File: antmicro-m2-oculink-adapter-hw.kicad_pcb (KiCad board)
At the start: 4 copper layers, 22 x 80 mm, 15 parts, among them J1 PCB-Edge_M.2_Key-M, J2 OCuLink_x4_Amphenol_G14A42121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

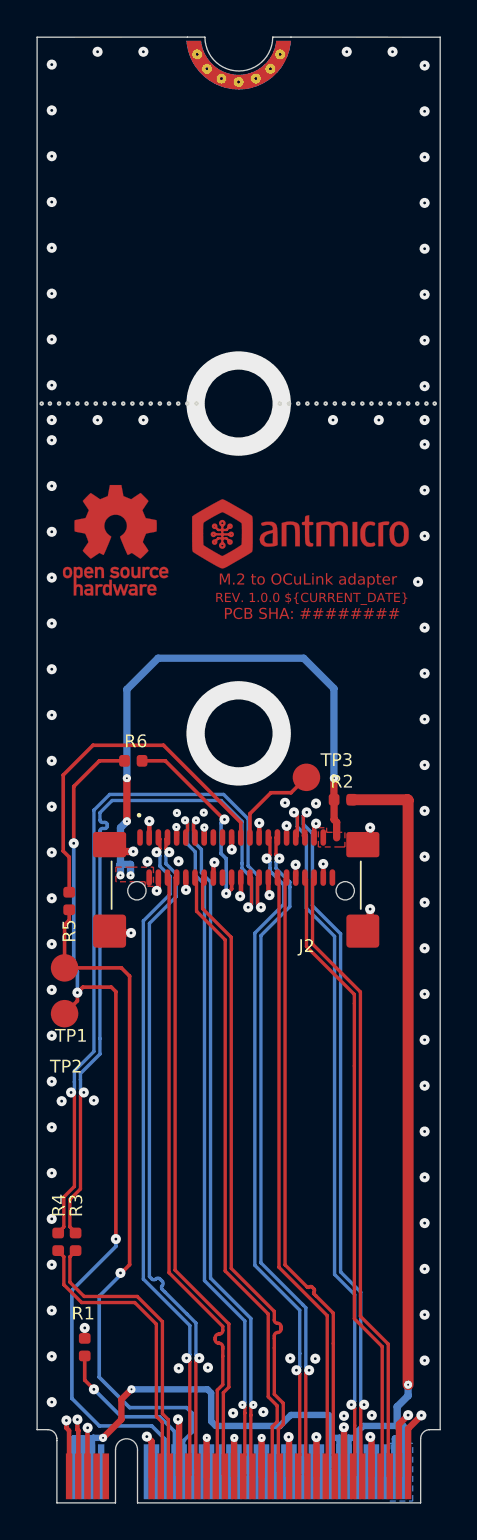
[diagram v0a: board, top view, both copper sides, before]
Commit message: [#80280] Clean up tracks, change gnd cutout size, fix drc errors, add more vias, move antmicro logo, change text size
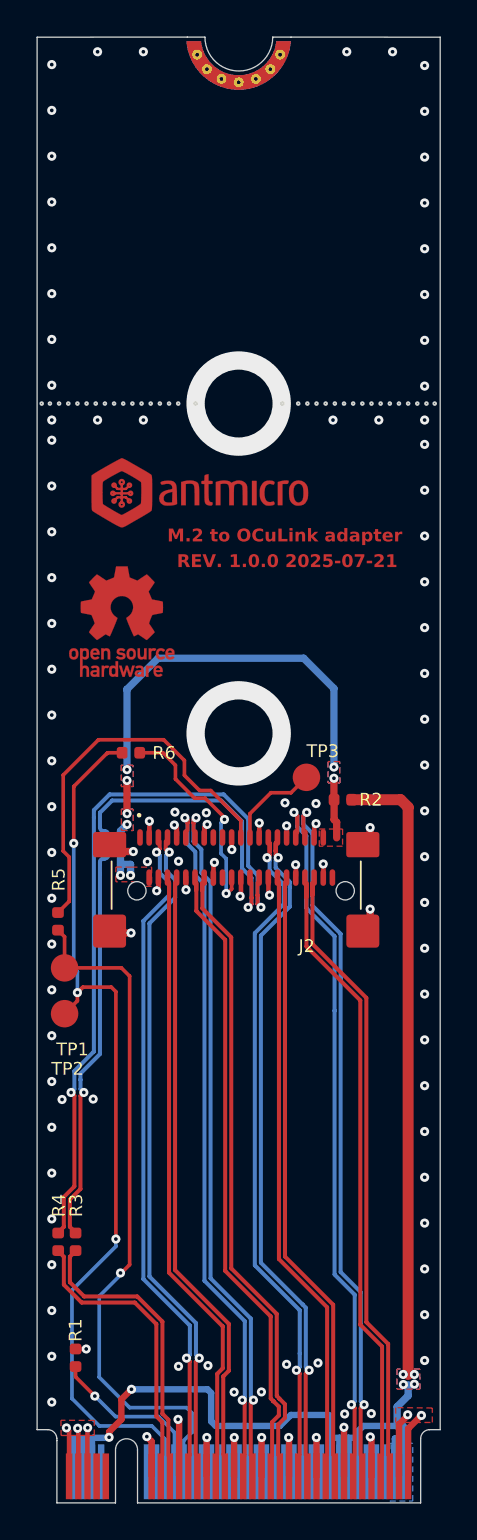
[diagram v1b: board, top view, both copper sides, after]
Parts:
- moved REF** 5.93 mm to (144.0, 75.5)
- moved REF** 4.45 mm to (139.8, 82.5) (x2)
- moved R5 1.27 mm to (136.3, 98.9)
- moved R1 0.77 mm to (137.2, 122.7)
- moved R6 0.46 mm to (140.3, 89.7)
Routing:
- net /~{PERSTC}: track 19.5 -> 21.6 mm
- net +3V3: track 32.5 -> 30.6 mm, vias 5 -> 8
- net /PCIe_{x4}.TX3+: track 39.3 -> 37.7 mm
- net /PCIe_{x4}.TX0+: track 37.1 -> 35.6 mm
- net /PCIe_{x4}.TX3-: track 39.2 -> 37.8 mm
- net /PCIe_{x4}.TX0-: track 37.1 -> 35.7 mm
- net /PCIe_{x4}.RX0-: track 34.1 -> 33.0 mm
- net /PCIe_{x4}.RX0+: track 34.1 -> 33.0 mm
- net /PCIe_{x4}.RX1+: track 34.8 -> 33.7 mm
- net /~{PERST}: track 38.9 -> 37.8 mm
- net /PCIe_{x4}.RX1-: track 34.7 -> 33.7 mm
- net /PCIe_{x4}.RX3-: track 34.6 -> 33.6 mm
- net /PCIe_{x4}.RX3+: track 34.6 -> 33.8 mm
- net /~{WAKEC}: track 11.2 -> 11.9 mm
- net Net-(J1-3.3V-Pad12): track 78.6 -> 78.0 mm, vias 3 -> 6
- added copper zone on B.Cu, net +3V3
- added copper zone on F.Cu, net GND
- added copper zone on F.Cu, net Net-(J1-3.3V-Pad12)
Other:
- outline, holes or cut-outs redrawn
- board text added: "REV. 1.0.0 2025-07-21"
- board text removed: "REV. ${REVISION} ${CURRENT_DATE}"

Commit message: [#80747] Clean up tracks
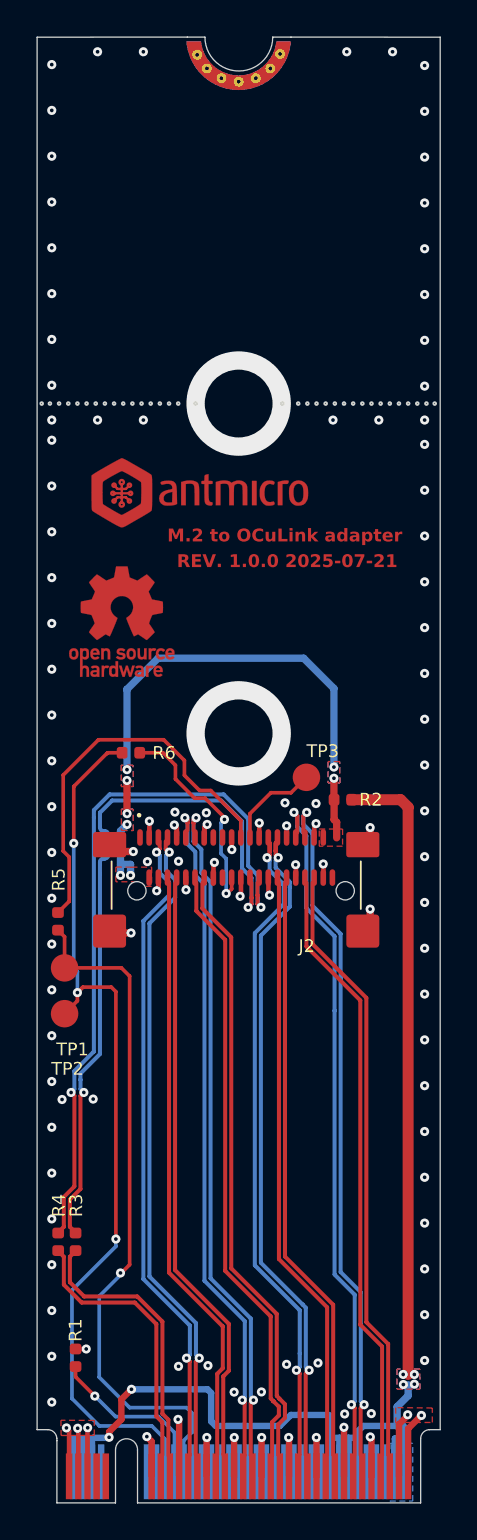
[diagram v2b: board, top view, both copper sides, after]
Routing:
- net /PCIe_{x4}.RX3+: track 33.8 -> 32.9 mm
- net /PCIe_{x4}.RX2+: track 33.1 -> 32.3 mm
- net /PCIe_{x4}.RX3-: track 33.6 -> 32.9 mm
- net /PCIe_{x4}.RX2-: track 33.0 -> 32.3 mm
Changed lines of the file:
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@@
 		)
 		(pad "1" thru_hole circle
-			(at -2.263505 0.937574)
+			(at -2.263505 0.947574)
 			(size 0.55 0.55)
 			(drill 0.2)
@@
 		)
 		(pad "1" thru_hole circle
-			(at -1.732412 1.732412)
+			(at -1.732412 1.692412)
 			(size 0.55 0.55)
 			(drill 0.2)
@@
 		)
 		(pad "1" thru_hole circle
-			(at -0.937574 2.263505)
+			(at -0.937574 2.223505)
 			(size 0.55 0.55)
 			(drill 0.2)
@@
 		)
 		(pad "1" thru_hole circle
-			(at 0 2.45)
+			(at 0 2.41)
 			(size 0.55 0.55)
 			(drill 0.2)
@@
 		)
 		(pad "1" smd custom
-			(at 0 2.45)
+			(at 0 2.46)
 			(size 0.55 0.55)
 			(layers "F.Cu" "F.Mask")
@@
 		)
 		(pad "1" smd custom
-			(at 0 2.45)
+			(at 0 2.46)
 			(size 0.55 0.55)
 			(layers "B.Cu" "B.Mask")
@@
 		)
 		(pad "1" thru_hole circle
-			(at 0.937574 2.263505)
+			(at 0.937574 2.223505)
 			(size 0.55 0.55)
 			(drill 0.2)
@@
 		)
 		(pad "1" thru_hole circle
-			(at 1.732412 1.732412)
+			(at 1.732412 1.692412)
 			(size 0.55 0.55)
 			(drill 0.2)
@@
 		)
 		(pad "1" thru_hole circle
-			(at 2.263505 0.937574)
+			(at 2.263505 0.897574)
 			(size 0.55 0.55)
 			(drill 0.2)
@@
 			(type default)
 		)
+		(locked yes)
 		(layer "Edge.Cuts")
 	)
@@
 			(type default)
 		)
+		(locked yes)
 		(layer "Edge.Cuts")
 	)
@@
 			(type default)
 		)
+		(locked yes)
 		(layer "Edge.Cuts")
 	)
@@
 			(type default)
 		)
+		(locked yes)
 		(layer "Edge.Cuts")
 	)
@@
 			(type default)
 		)
+		(locked yes)
 		(layer "Edge.Cuts")
 	)
@@
 	)
 	(segment
-		(start 148.35 96.75553)
-		(end 148.35 97.564469)
-		(width 0.22)
-		(layer "F.Cu")
-		(net 4)
-	)
-	(segment
 		(start 148.35 117.293346)
 		(end 150.98 119.923346)
@@
 	)
 	(segment
-		(start 150.18 97.438185)
-		(end 150.18 96.75553)
-		(width 0.22)
-		(layer "F.Cu")
-		(net 6)
-	)
-	(segment
 		(start 153.12 103.036654)
 		(end 153.12 120.736654)
@@
 	)
 	(segment
-		(start 142.68 97.180012)
-		(end 142.68 96.76)
-		(width 0.22)
-		(layer "F.Cu")
-		(net 7)
-	)
-	(segment
 		(start 142.68 117.896654)
 		(end 145.615 120.831654)
@@
 	)
 	(segment
-		(start 149.85 97.564469)
-		(end 149.85 96.75553)
-		(width 0.22)
-		(layer "F.Cu")
-		(net 9)
-	)
-	(segment
 		(start 153.979 122.062346)
 		(end 153.979 127.989345)
@@
 	(segment
 		(start 148.68 96.75553)
-		(end 148.68 97.438185)
-		(width 0.22)
-		(layer "F.Cu")
-		(net 14)
-	)
-	(segment
-		(start 148.68 96.75553)
 		(end 148.68 117.156654)
 		(width 0.22)
@@
 	)
 	(segment
-		(start 143.84 97.16475)
-		(end 143.84 96.759988)
-		(width 0.22)
-		(layer "F.Cu")
-		(net 16)
-	)
-	(segment
 		(start 147.899 124.897105)
 		(end 148.0445 125.042604)
@@
 	)
 	(segment
-		(start 142.35 97.164762)
-		(end 142.35 96.76)
-		(width 0.22)
-		(layer "F.Cu")
-		(net 27)
-	)
-	(segment
 		(start 148.3755 124.911448)
 		(end 148.6755 125.211448)
@@
 		(width 0.22)
 		(layer "F.Cu")
-		(net 28)
-	)
-	(segment
-		(start 144.17 97.18)
-		(end 144.17 96.759988)
-		(width 0.22)
-		(layer "F.Cu")

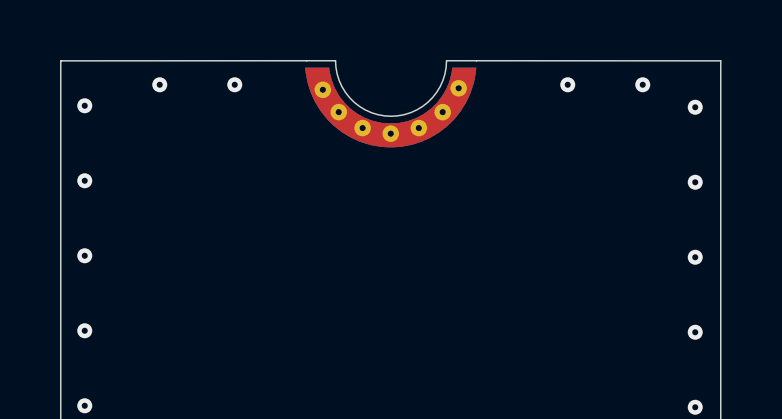
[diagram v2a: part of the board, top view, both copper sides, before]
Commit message: [#80747] Replace edge drill footprint
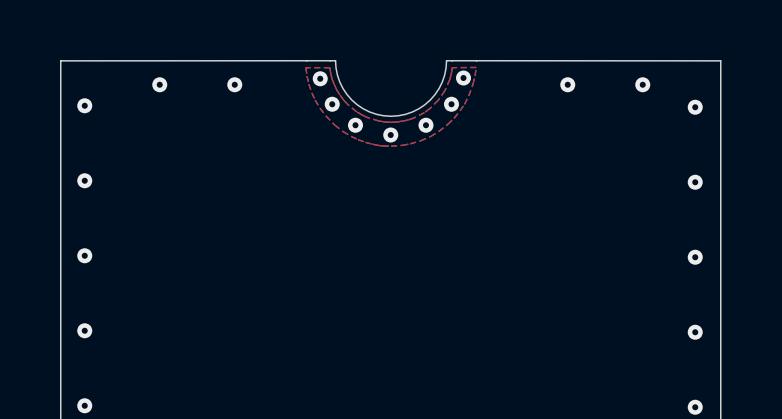
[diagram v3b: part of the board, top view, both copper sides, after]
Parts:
- removed the REF** at (146.2, 50.6)
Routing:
- net GND: vias 120 -> 127
- added copper zone on B.Cu, net GND
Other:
- outline, holes or cut-outs redrawn

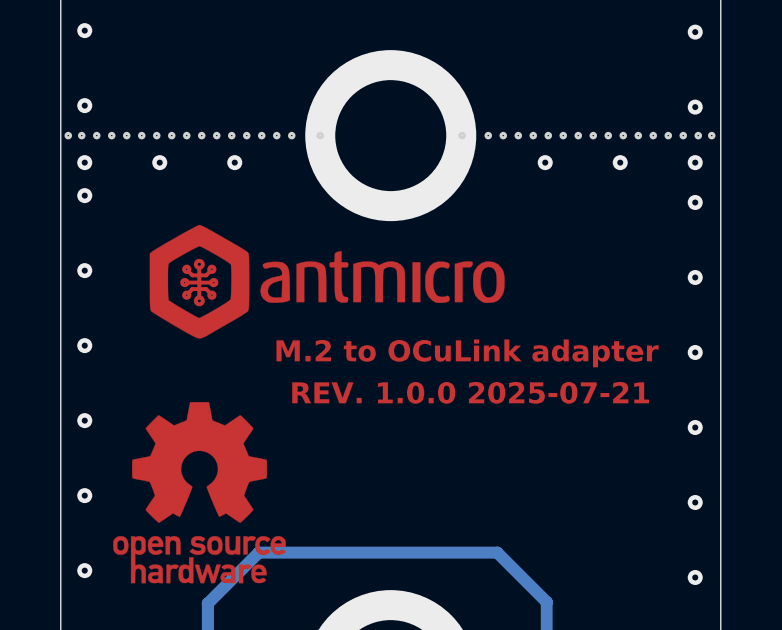
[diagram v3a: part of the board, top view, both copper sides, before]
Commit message: [#80747] change antmicro logo and correct date format
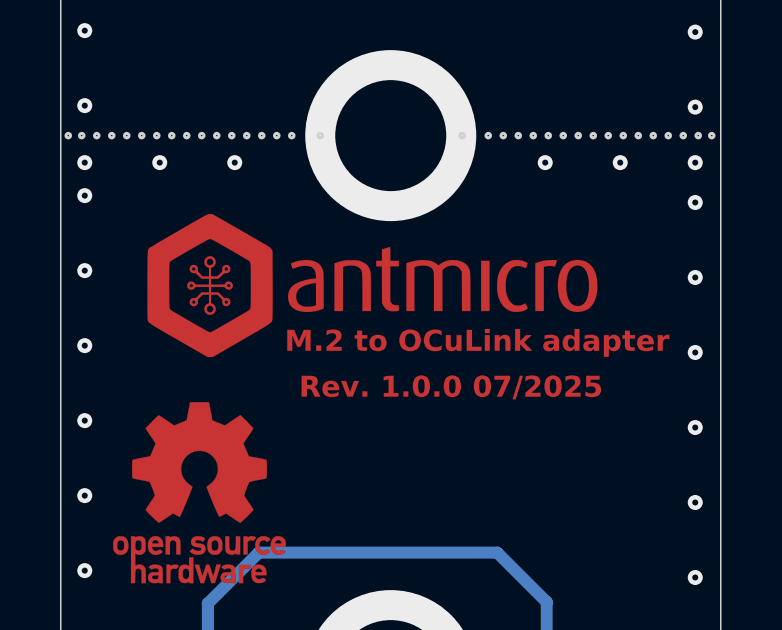
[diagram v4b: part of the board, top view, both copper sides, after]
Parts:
- removed the REF** at (144.0, 75.5)
- added REF**: antmicro-logo_scaled_15mm, antmicro-footprints:antmicro-logo_scaled_15mm, F.Cu at (146.0, 75.7)
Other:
- board text added: "Rev. 1.0.0 07/2025"
- board text removed: "REV. 1.0.0 2025-07-21"

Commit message: [#80747] Fix DRC
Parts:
- moved REF** 1.06 mm to (140.2, 83.5) (x2)
- moved REF** 0.28 mm to (146.0, 75.4)
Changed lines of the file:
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@@
 	(footprint "antmicro-footprints:antmicro-logo_scaled_15mm"
 		(layer "F.Cu")
-		(at 145.99 75.67)
+		(at 146.005 75.395)
 		(property "Reference" "REF**"
 			(at 0.1 -3 0)
@@
 	(footprint "antmicro-footprints:OSHW-Logo_5.7x6mm_Mask"
 		(layer "F.Cu")
-		(at 139.77 82.5)
+		(at 140.175 83.475)
 		(descr "Open Source Hardware Logo")
 		(tags "Logo OSHW")
@@
 	(footprint "antmicro-footprints:OSHW-Logo_5.7x6mm_Copper"
 		(layer "F.Cu")
-		(at 139.77 82.5)
+		(at 140.175 83.475)
 		(descr "Open Source Hardware Logo")
 		(tags "Logo OSHW")
@@
 	)
 	(gr_text "${TITLE}"
-		(at 148.86 77.45 0)
+		(at 148.65 77.25 0)
 		(layer "F.Cu")
 		(effects
@@
 	)
 	(gr_text "Rev. 1.0.0 07/2025\n"
-		(at 148.16 78.98 0)
+		(at 147.975 78.65 0)
 		(layer "F.Cu")
 		(effects
@@
 	)
 	(gr_text "${TITLE}"
-		(at 148.86 77.45 0)
+		(at 148.65 77.25 0)
 		(layer "F.Mask")
 		(effects
@@
 	)
 	(gr_text "Rev. 1.0.0 07/2025\n"
-		(at 148.16 78.98 0)
+		(at 147.975 78.65 0)
 		(layer "F.Mask")
 		(effects
